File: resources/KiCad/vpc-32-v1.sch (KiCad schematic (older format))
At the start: 46 parts, among them J1 video out, J2 SD_SOCKET, J3 PS/2, J4 audio out, K1 jumper, P1 CONN_2, P2 ICSP, P3 XBUS, Q1 2N3906, Q2 2N3094, SW1 reset, U1 PIC32MX150F128B, U2 LM3940-3.3, X1 10Mhz

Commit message: ajout licence Creative Commons au projet KiCad
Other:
- note added: "Copyright 2013, Jacques Deschênes\nlicence Creative Commons: CC BY-SA"
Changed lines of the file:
@@
-EESchema Schematic File Version 2  date 2013-08-25 22:04:50
+EESchema Schematic File Version 2  date 2013-08-27 09:48:55
 LIBS:power
 LIBS:device
@@
 Sheet 1 1
 Title ""
-Date "26 aug 2013"
+Date "27 aug 2013"
 Rev ""
 Comp ""
@@
 Wire Wire Line
 	8550 1950 8550 2600
+Text Notes 7050 7050 0    59   ~ 0
+Copyright 2013, Jacques Deschênes\nlicence Creative Commons: CC BY-SA
 $EndSCHEMATC

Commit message: réglé bug avec interrupton TIMER 2
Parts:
- added D?: Power, symbol LED
- added D?: Status LED, symbol LED
- added R?: 150R, symbol R
- added R?: 220R, symbol R
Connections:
- net labels added: RB1, STATUS
- net labels removed: RB3, ~U2RTS
- wire segments 123 -> 128
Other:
- note added: "2"
- note removed: "1"
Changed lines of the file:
@@
-EESchema Schematic File Version 2  date 2013-08-27 09:48:55
+EESchema Schematic File Version 2  date 2013-08-28 16:27:26
 LIBS:power
 LIBS:device
@@
 Sheet 1 1
 Title ""
-Date "27 aug 2013"
+Date "28 aug 2013"
 Rev ""
 Comp ""
@@
 Connection ~ 4400 6150
 Wire Wire Line
-	2850 6150 4400 6150
+	2850 6150 4550 6150
 Wire Wire Line
 	8500 4700 8500 4900
@@
 RB0
 Text GLabel 6250 5800 0    39   Input ~ 0
-RB3
+RB1
 Text GLabel 6250 5900 0    39   Input ~ 0
 RB8
@@
 VPC-32
 Text Notes 10700 7650 0    59   ~ 0
-1
+2
 $Comp
 L R R8
@@
 Wire Wire Line
 	7850 1600 8050 1600
-Text GLabel 4950 3650 0    39   Input ~ 0
-~U2RTS
-Wire Wire Line
-	4950 3650 5100 3650
 $Comp
 L RJ11 J?
@@
 Text Notes 7050 7050 0    59   ~ 0
 Copyright 2013, Jacques Deschênes\nlicence Creative Commons: CC BY-SA
+$Comp
+L LED D?
+U 1 1 521E10B9
+P 5150 6350
+F 0 "D?" H 5150 6450 50  0000 C CNN
+F 1 "Power" H 5150 6250 50  0000 C CNN
+F 2 "" H 5150 6350 60  0000 C CNN
+F 3 "" H 5150 6350 60  0000 C CNN
+	1    5150 6350
+	0    1    1    0
+$EndComp
+$Comp
+L R R?
+U 1 1 521E10C8
+P 4800 6150
+F 0 "R?" V 4880 6150 50  0000 C CNN
+F 1 "150R" V 4800 6150 50  0000 C CNN
+F 2 "" H 4800 6150 60  0000 C CNN
+F 3 "" H 4800 6150 60  0000 C CNN
+	1    4800 6150
+	0    -1   -1   0
+$EndComp
+$Comp
+L GND #PWR?
+U 1 1 521E10D5
+P 5150 6650
+F 0 "#PWR?" H 5150 6650 30  0001 C CNN
+F 1 "GND" H 5150 6580 30  0001 C CNN
+F 2 "" H 5150 6650 60  0000 C CNN
+F 3 "" H 5150 6650 60  0000 C CNN
+	1    5150 6650
+	1    0    0    -1
+$EndComp
+Wire Wire Line
+	5050 6150 5150 6150
+Wire Wire Line
+	5150 6550 5150 6650
+$Comp
+L LED D?
+U 1 1 521E127D
+P 4200 5350
+F 0 "D?" H 4200 5450 50  0000 C CNN
+F 1 "Status LED" H 4200 5250 50  0000 C CNN
+F 2 "" H 4200 5350 60  0000 C CNN
+F 3 "" H 4200 5350 60  0000 C CNN
+	1    4200 5350
+	0    1    1    0
+$EndComp
+$Comp
+L R R?
+U 1 1 521E128C
+P 3950 5000
+F 0 "R?" V 4030 5000 50  0000 C CNN
+F 1 "220R" V 3950 5000 50  0000 C CNN
+F 2 "" H 3950 5000 60  0000 C CNN
+F 3 "" H 3950 5000 60  0000 C CNN
+	1    3950 5000
+	0    -1   -1   0
+$EndComp
+$Comp
+L GND #PWR?
+U 1 1 521E12A3
+P 4200 5650
+F 0 "#PWR?" H 4200 5650 30  0001 C CNN
+F 1 "GND" H 4200 5580 30  0001 C CNN
+F 2 "" H 4200 5650 60  0000 C CNN
+F 3 "" H 4200 5650 60  0000 C CNN
+	1    4200 5650
+	1    0    0    -1
+$EndComp
+Text GLabel 5050 3650 0    39   Input ~ 0
+STATUS
+Wire Wire Line
+	5100 3650 5050 3650
+Text GLabel 3600 5000 0    39   Input ~ 0
+STATUS
+Wire Wire Line
+	4200 5550 4200 5650
+Wire Wire Line
+	4200 5000 4200 5150
+Wire Wire Line
+	3700 5000 3600 5000
 $EndSCHEMATC

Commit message: modification au schéma électronique
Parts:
- removed R7: 10k, symbol R
- gave numbers to parts that had none: 5
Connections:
- net labels removed: V+
- wire segments 128 -> 129
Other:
- moved on the sheet: J5
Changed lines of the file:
@@
-EESchema Schematic File Version 2  date 2013-08-28 16:27:26
+EESchema Schematic File Version 2  date 2013-09-01 22:06:51
 LIBS:power
 LIBS:device
@@
 Sheet 1 1
 Title ""
-Date "28 aug 2013"
+Date "2 sep 2013"
 Rev ""
 Comp ""
@@
 $EndComp
 $Comp
-L GND #PWR6
+L GND #PWR01
 U 1 1 52181107
 P 3550 4650
-F 0 "#PWR6" H 3550 4650 30  0001 C CNN
+F 0 "#PWR01" H 3550 4650 30  0001 C CNN
 F 1 "GND" H 3550 4580 30  0001 C CNN
 F 2 "" H 3550 4650 60  0000 C CNN
@@
 $EndComp
 $Comp
-L GND #PWR9
+L GND #PWR02
 U 1 1 52181114
 P 4150 4650
-F 0 "#PWR9" H 4150 4650 30  0001 C CNN
+F 0 "#PWR02" H 4150 4650 30  0001 C CNN
 F 1 "GND" H 4150 4580 30  0001 C CNN
 F 2 "" H 4150 4650 60  0000 C CNN
@@
 $EndComp
 $Comp
-L GND #PWR17
+L GND #PWR03
 U 1 1 52181145
 P 8500 4900
-F 0 "#PWR17" H 8500 4900 30  0001 C CNN
+F 0 "#PWR03" H 8500 4900 30  0001 C CNN
 F 1 "GND" H 8500 4830 30  0001 C CNN
 F 2 "" H 8500 4900 60  0000 C CNN
@@
 +3,3V
 $Comp
-L GND #PWR14
+L GND #PWR04
 U 1 1 521812CB
 P 7000 4000
-F 0 "#PWR14" H 7000 4000 30  0001 C CNN
+F 0 "#PWR04" H 7000 4000 30  0001 C CNN
 F 1 "GND" H 7000 3930 30  0001 C CNN
 F 2 "" H 7000 4000 60  0000 C CNN
@@
 $EndComp
 $Comp
-L GND #PWR12
+L GND #PWR05
 U 1 1 521812EF
 P 4850 3750
-F 0 "#PWR12" H 4850 3750 30  0001 C CNN
+F 0 "#PWR05" H 4850 3750 30  0001 C CNN
 F 1 "GND" H 4850 3680 30  0001 C CNN
 F 2 "" H 4850 3750 60  0000 C CNN
@@
 $EndComp
 $Comp
-L GND #PWR8
+L GND #PWR06
 U 1 1 52181391
 P 3950 6650
-F 0 "#PWR8" H 3950 6650 30  0001 C CNN
+F 0 "#PWR06" H 3950 6650 30  0001 C CNN
 F 1 "GND" H 3950 6580 30  0001 C CNN
 F 2 "" H 3950 6650 60  0000 C CNN
@@
 $EndComp
 $Comp
-L GND #PWR10
+L GND #PWR07
 U 1 1 52181397
 P 4400 6650
-F 0 "#PWR10" H 4400 6650 30  0001 C CNN
+F 0 "#PWR07" H 4400 6650 30  0001 C CNN
 F 1 "GND" H 4400 6580 30  0001 C CNN
 F 2 "" H 4400 6650 60  0000 C CNN
@@
 $EndComp
 $Comp
-L GND #PWR5
+L GND #PWR08
 U 1 1 5218D55D
 P 3300 2800
-F 0 "#PWR5" H 3300 2800 30  0001 C CNN
+F 0 "#PWR08" H 3300 2800 30  0001 C CNN
 F 1 "GND" H 3300 2730 30  0001 C CNN
 F 2 "" H 3300 2800 60  0000 C CNN
@@
 $EndComp
 $Comp
-L GND #PWR15
+L GND #PWR09
 U 1 1 521A0F8C
 P 7400 4000
-F 0 "#PWR15" H 7400 4000 30  0001 C CNN
+F 0 "#PWR09" H 7400 4000 30  0001 C CNN
 F 1 "GND" H 7400 3930 30  0001 C CNN
 F 2 "" H 7400 4000 60  0000 C CNN
@@
 $EndComp
 $Comp
-L GND #PWR7
+L GND #PWR010
 U 1 1 521A102C
 P 3750 1800
-F 0 "#PWR7" H 3750 1800 30  0001 C CNN
+F 0 "#PWR010" H 3750 1800 30  0001 C CNN
 F 1 "GND" H 3750 1730 30  0001 C CNN
 F 2 "" H 3750 1800 60  0000 C CNN
@@
 $EndComp
 $Comp
-L GND #PWR11
+L GND #PWR011
 U 1 1 521A10AE
 P 4600 2450
-F 0 "#PWR11" H 4600 2450 30  0001 C CNN
+F 0 "#PWR011" H 4600 2450 30  0001 C CNN
 F 1 "GND" H 4600 2380 30  0001 C CNN
 F 2 "" H 4600 2450 60  0000 C CNN
@@
 $EndComp
 $Comp
-L GND #PWR4
+L GND #PWR012
 U 1 1 521A15C0
 P 3100 4800
-F 0 "#PWR4" H 3100 4800 30  0001 C CNN
+F 0 "#PWR012" H 3100 4800 30  0001 C CNN
 F 1 "GND" H 3100 4730 30  0001 C CNN
 F 2 "" H 3100 4800 60  0000 C CNN
@@
 	1    0    0    -1
 $EndComp
-Text GLabel 3250 4200 1    60   Input ~ 0
-V+
+Text GLabel 3250 4200 1    39   Input ~ 0
++3,3V
 Text GLabel 2750 4550 2    39   Input ~ 0
 SPI2/SDI
@@
 F 3 "" H 1750 3550 60  0000 C CNN
 	1    1750 3550
-	1    0    0    -1
-$EndComp
-$Comp
-L R R7
-U 1 1 521A1B35
-P 2150 3550
-F 0 "R7" V 2230 3550 50  0000 C CNN
-F 1 "10k" V 2150 3550 50  0000 C CNN
-F 2 "" H 2150 3550 60  0000 C CNN
-F 3 "" H 2150 3550 60  0000 C CNN
-	1    2150 3550
 	1    0    0    -1
 $EndComp
@@
 +3,3V
 $Comp
-L GND #PWR13
+L GND #PWR013
 U 1 1 521A28F4
 P 6000 1650
-F 0 "#PWR13" H 6000 1650 30  0001 C CNN
+F 0 "#PWR013" H 6000 1650 30  0001 C CNN
 F 1 "GND" H 6000 1580 30  0001 C CNN
 F 2 "" H 6000 1650 60  0000 C CNN
@@
 PGEC1
 $Comp
-L GND #PWR22
+L GND #PWR014
 U 1 1 521A78A1
 P 9750 2600
-F 0 "#PWR22" H 9750 2600 30  0001 C CNN
+F 0 "#PWR014" H 9750 2600 30  0001 C CNN
 F 1 "GND" H 9750 2530 30  0001 C CNN
 F 2 "" H 9750 2600 60  0000 C CNN
@@
 Wire Wire Line
 	1750 3300 1750 3200
-Wire Wire Line
-	1750 3300 2150 3300
 Wire Wire Line
 	1750 4750 2150 4750
@@
 $EndComp
 Wire Wire Line
-	9750 2300 9050 2300
-Wire Wire Line
 	8850 2800 9050 2800
 $Comp
@@
 $EndComp
 $Comp
-L GND #PWR19
+L GND #PWR015
 U 1 1 521A7A94
 P 8550 3100
-F 0 "#PWR19" H 8550 3100 30  0001 C CNN
+F 0 "#PWR015" H 8550 3100 30  0001 C CNN
 F 1 "GND" H 8550 3030 30  0001 C CNN
 F 2 "" H 8550 3100 60  0000 C CNN
@@
 $EndComp
 $Comp
-L GND #PWR23
+L GND #PWR016
 U 1 1 521A7A9A
 P 9550 2950
-F 0 "#PWR23" H 9550 2950 30  0001 C CNN
+F 0 "#PWR016" H 9550 2950 30  0001 C CNN
 F 1 "GND" H 9550 2880 30  0001 C CNN
 F 2 "" H 9550 2950 60  0000 C CNN
@@
 	7850 2300 8650 2300
 $Comp
-L GND #PWR18
+L GND #PWR017
 U 1 1 521A7BF6
 P 8150 2850
-F 0 "#PWR18" H 8150 2850 30  0001 C CNN
+F 0 "#PWR017" H 8150 2850 30  0001 C CNN
 F 1 "GND" H 8150 2780 30  0001 C CNN
 F 2 "" H 8150 2850 60  0000 C CNN
@@
 TX
 Connection ~ 7850 1600
-Text GLabel 9600 2150 0    39   Input ~ 0
+Text GLabel 9550 2000 0    39   Input ~ 0
 TX
 Text GLabel 6700 3750 2    39   Input ~ 0
@@
 $EndComp
 $Comp
-L GND #PWR24
+L GND #PWR018
 U 1 1 521A9812
 P 10500 6350
-F 0 "#PWR24" H 10500 6350 30  0001 C CNN
+F 0 "#PWR018" H 10500 6350 30  0001 C CNN
 F 1 "GND" H 10500 6280 30  0001 C CNN
 F 2 "" H 10500 6350 60  0000 C CNN
@@
 	10500 6200 10500 6350
 $Comp
-L GND #PWR21
+L GND #PWR019
 U 1 1 521A9A38
 P 9750 6450
-F 0 "#PWR21" H 9750 6450 30  0001 C CNN
+F 0 "#PWR019" H 9750 6450 30  0001 C CNN
 F 1 "GND" H 9750 6380 30  0001 C CNN
 F 2 "" H 9750 6450 60  0000 C CNN
@@
 $EndComp
 $Comp
-L GND #PWR20
+L GND #PWR020
 U 1 1 521A9A3E
 P 9250 6450
-F 0 "#PWR20" H 9250 6450 30  0001 C CNN
+F 0 "#PWR020" H 9250 6450 30  0001 C CNN
 F 1 "GND" H 9250 6380 30  0001 C CNN
 F 2 "" H 9250 6450 60  0000 C CNN
@@
 $EndComp
 $Comp
-L GND #PWR16
+L GND #PWR021
 U 1 1 521A9A4E
 P 8450 6450
-F 0 "#PWR16" H 8450 6450 30  0001 C CNN
+F 0 "#PWR021" H 8450 6450 30  0001 C CNN
 F 1 "GND" H 8450 6380 30  0001 C CNN
 F 2 "" H 8450 6450 60  0000 C CNN
@@
 $EndComp
 $Comp
-L GND #PWR3
+L GND #PWR022
 U 1 1 521A9D5C
 P 2700 6400
-F 0 "#PWR3" H 2700 6400 30  0001 C CNN
+F 0 "#PWR022" H 2700 6400 30  0001 C CNN
 F 1 "GND" H 2700 6330 30  0001 C CNN
 F 2 "" H 2700 6400 60  0000 C CNN
@@
 $EndComp
 $Comp
-L GND #PWR1
+L GND #PWR023
 U 1 1 521A9ED6
 P 1650 6500
-F 0 "#PWR1" H 1650 6500 30  0001 C CNN
+F 0 "#PWR023" H 1650 6500 30  0001 C CNN
 F 1 "GND" H 1650 6430 30  0001 C CNN
 F 2 "" H 1650 6500 60  0000 C CNN
@@
 $EndComp
 $Comp
-L GND #PWR2
+L GND #PWR024
 U 1 1 521AA1E5
 P 1900 6650
-F 0 "#PWR2" H 1900 6650 30  0001 C CNN
+F 0 "#PWR024" H 1900 6650 30  0001 C CNN
 F 1 "GND" H 1900 6580 30  0001 C CNN
 F 2 "" H 1900 6650 60  0000 C CNN
@@
 	7850 1600 8050 1600
 $Comp
-L RJ11 J?
+L RJ11 J5
 U 1 1 521AB1B3
-P 10350 2200
-F 0 "J?" H 10350 1850 60  0000 C CNN
-F 1 "RJ11" H 10300 2550 60  0000 C CNN
-F 2 "" H 10350 2200 60  0000 C CNN
-F 3 "" H 10350 2200 60  0000 C CNN
-	1    10350 2200
-	-1   0    0    1
+P 10350 2250
+F 0 "J5" H 10350 1900 60  0000 C CNN
+F 1 "RJ11" H 10300 2600 60  0000 C CNN
+F 2 "" H 10350 2250 60  0000 C CNN
+F 3 "" H 10350 2250 60  0000 C CNN
+	1    10350 2250
+	-1   0    0    -1
 $EndComp
 Wire Wire Line
 	9750 2600 9750 2450
 Wire Wire Line
-	9750 2150 9600 2150
+	9050 2150 9750 2150
 Wire Wire Line
 	8550 1950 8550 2600
@@
 Copyright 2013, Jacques Deschênes\nlicence Creative Commons: CC BY-SA
 $Comp
-L LED D?
+L LED D5
 U 1 1 521E10B9
 P 5150 6350
-F 0 "D?" H 5150 6450 50  0000 C CNN
+F 0 "D5" H 5150 6450 50  0000 C CNN
 F 1 "Power" H 5150 6250 50  0000 C CNN
 F 2 "" H 5150 6350 60  0000 C CNN
@@
 $EndComp
 $Comp
-L R R?
+L R R19
 U 1 1 521E10C8
 P 4800 6150
-F 0 "R?" V 4880 6150 50  0000 C CNN
+F 0 "R19" V 4880 6150 50  0000 C CNN
 F 1 "150R" V 4800 6150 50  0000 C CNN
 F 2 "" H 4800 6150 60  0000 C CNN
@@
 $EndComp
 $Comp
-L GND #PWR?
+L GND #PWR025
 U 1 1 521E10D5
 P 5150 6650
-F 0 "#PWR?" H 5150 6650 30  0001 C CNN
+F 0 "#PWR025" H 5150 6650 30  0001 C CNN
 F 1 "GND" H 5150 6580 30  0001 C CNN
 F 2 "" H 5150 6650 60  0000 C CNN
@@
 	5150 6550 5150 6650
 $Comp
-L LED D?
+L LED D4
 U 1 1 521E127D
 P 4200 5350
-F 0 "D?" H 4200 5450 50  0000 C CNN
+F 0 "D4" H 4200 5450 50  0000 C CNN
 F 1 "Status LED" H 4200 5250 50  0000 C CNN
 F 2 "" H 4200 5350 60  0000 C CNN
@@
 $EndComp
 $Comp
-L R R?
+L R R18
 U 1 1 521E128C
 P 3950 5000
-F 0 "R?" V 4030 5000 50  0000 C CNN
+F 0 "R18" V 4030 5000 50  0000 C CNN
 F 1 "220R" V 3950 5000 50  0000 C CNN
 F 2 "" H 3950 5000 60  0000 C CNN
@@
 $EndComp
 $Comp
-L GND #PWR?
+L GND #PWR026
 U 1 1 521E12A3
 P 4200 5650
-F 0 "#PWR?" H 4200 5650 30  0001 C CNN
+F 0 "#PWR026" H 4200 5650 30  0001 C CNN
 F 1 "GND" H 4200 5580 30  0001 C CNN
 F 2 "" H 4200 5650 60  0000 C CNN
@@
 Wire Wire Line
 	3700 5000 3600 5000
+Wire Wire Line
+	2150 3800 1750 3800
+Wire Wire Line
+	9550 2000 9750 2000
+Wire Wire Line
+	9050 2300 9050 2150
 $EndSCHEMATC

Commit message: ajout photos prototype
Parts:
- removed P3: XBUS, symbol CONN_6
- added P3: XBUS, symbol CONN_5
- added R?: 22k, symbol R
- R6: value 10k -> 22k
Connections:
- net labels added: SDO2
- net labels removed: RB8
- wire segments 129 -> 131
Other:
- moved on the sheet: R6

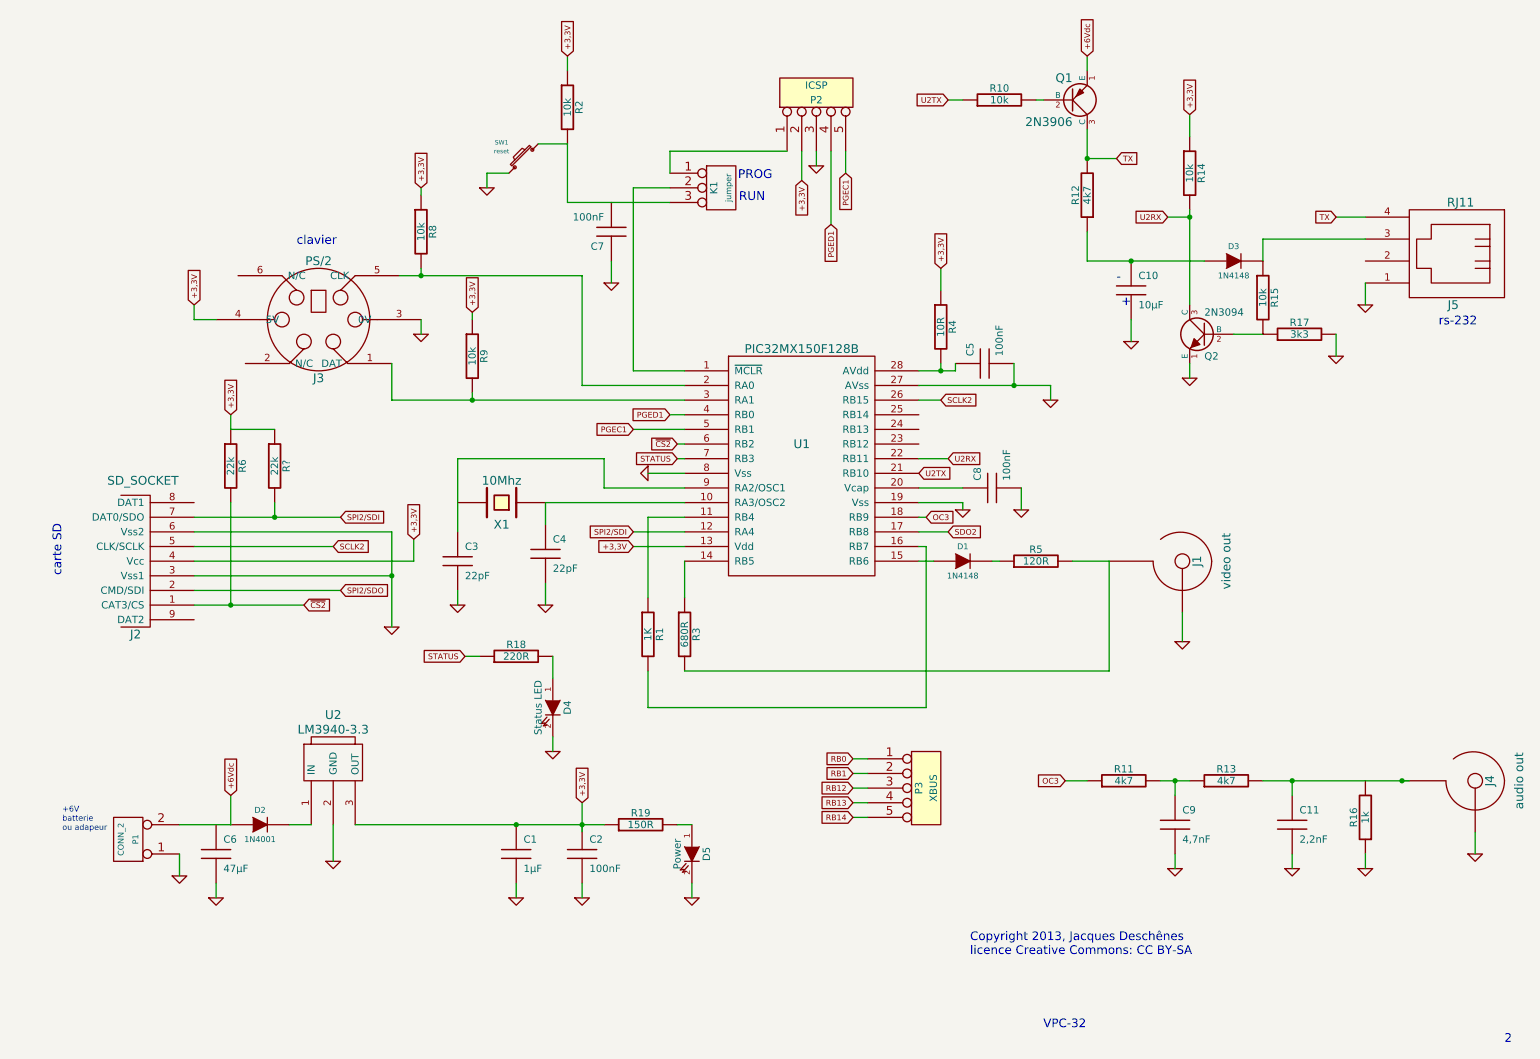
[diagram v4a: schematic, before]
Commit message: modification au schéma électronique, test interface RS-232
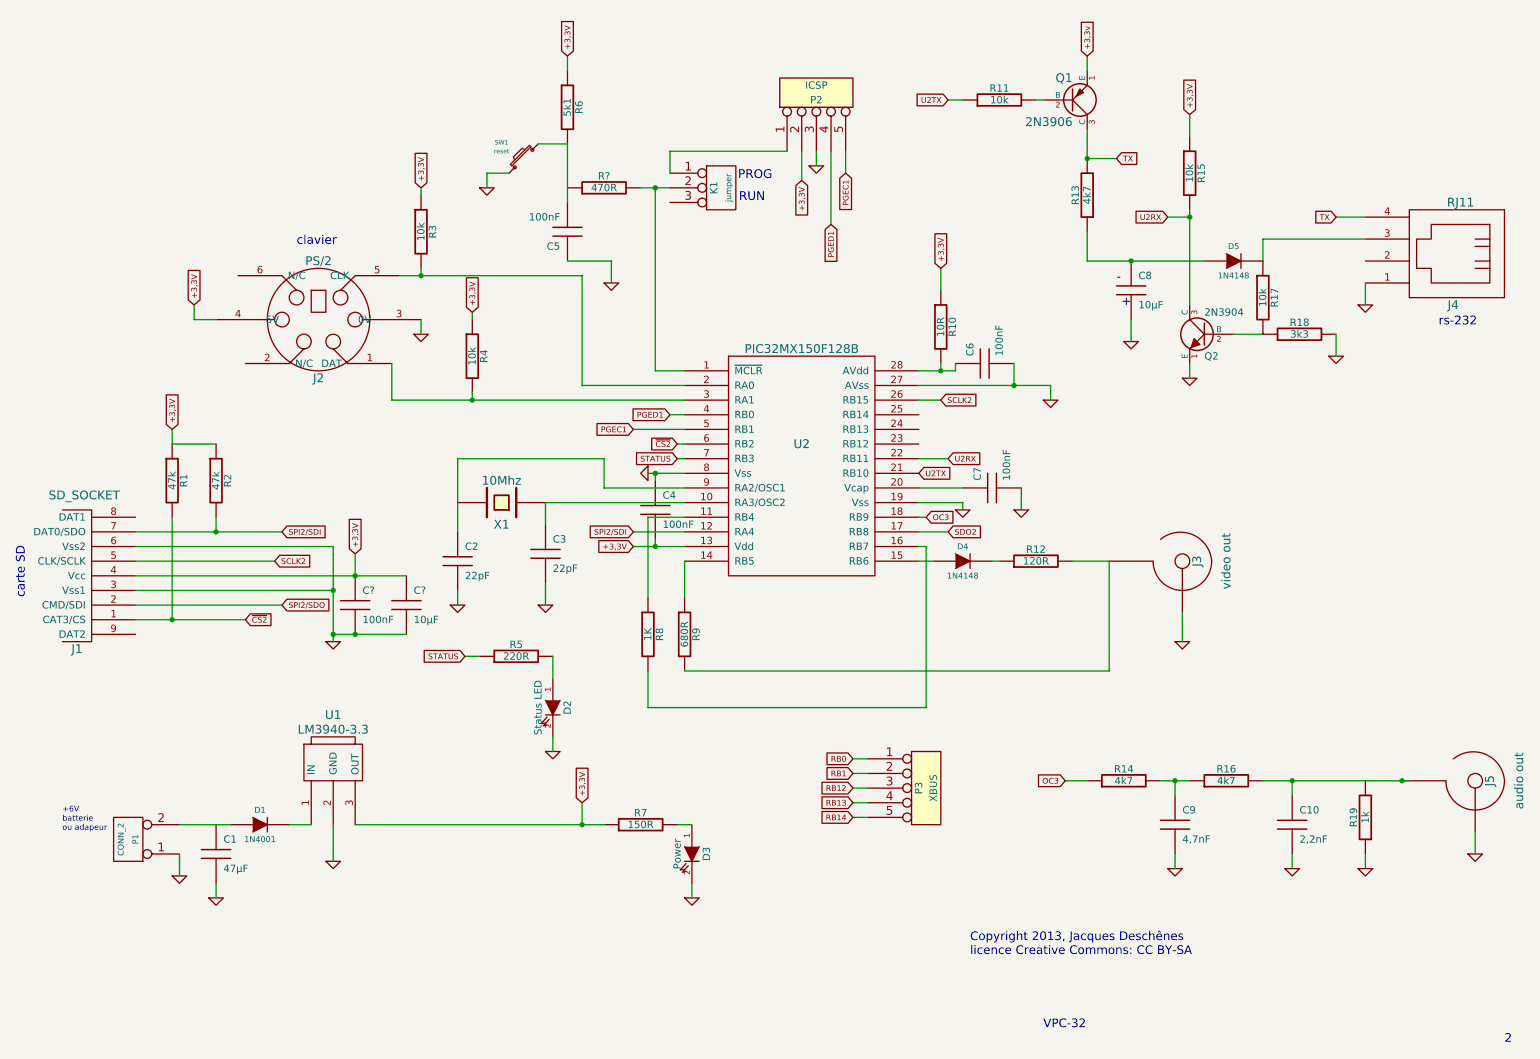
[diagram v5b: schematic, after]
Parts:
- removed C1: 1µF, symbol C
- added C?: 100nF, symbol C
- added C?: 10µF, symbol C
- added R?: 470R, symbol R
- Q2: value 2N3094 -> 2N3904
- R1: renamed from R6; value 22k -> 47k
- R2: renamed from R?; value 22k -> 47k
- R6: renamed from R2; value 10k -> 5k1
- renumbered C6 to C1, C11 to C10, C3 to C2, C4 to C3, C2 to C4, C7 to C5, C5 to C6, C8 to C7, C10 to C8, D2 to D1, D4 to D2, D5 to D3, D1 to D4, D3 to D5, J2 to J1, J3 to J2, J1 to J3, J5 to J4, J4 to J5, R4 to R10, R10 to R11, R5 to R12, R12 to R13, R11 to R14, R14 to R15, R13 to R16, R15 to R17, R17 to R18, R16 to R19, R8 to R3, R9 to R4, R18 to R5, R19 to R7, R1 to R8, R3 to R9, U2 to U1, U1 to U2
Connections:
- net +3,3V: now also C4.2, C?.1, C?.1; no longer C4.1
- net GND: now also C4.1, C?.2, C?.2; no longer C4.2
- net at K1.2 (PM), U2.1 (~MCLR): now also R?.2
- net at R6.2, SW1.1: now also C5.2; no longer K1.3 (P3)
- net +6Vdc: no longer names the net of D1.1 (A), P1.2 (PM)
- net +6Vdc: no longer Q1.1 (E)
- new net +3,3v: Q1.1 (E)
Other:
- moved on the sheet: C4, C5, J1, R1, R2

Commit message: travail sur graphics.c
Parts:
- R6: value 5k1 -> 22k
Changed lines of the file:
@@
-EESchema Schematic File Version 2  date 2013-09-05 09:54:04
+EESchema Schematic File Version 2  date 2013-10-02 07:50:32
 LIBS:power
 LIBS:device
@@
 Sheet 1 1
 Title ""
-Date "5 sep 2013"
+Date "2 oct 2013"
 Rev ""
 Comp ""
@@
 P 4300 1250
 F 0 "R6" V 4380 1250 50  0000 C CNN
-F 1 "5k1" V 4300 1250 50  0000 C CNN
+F 1 "22k" V 4300 1250 50  0000 C CNN
 F 2 "" H 4300 1250 60  0000 C CNN
 F 3 "" H 4300 1250 60  0000 C CNN

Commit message: work on shell
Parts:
- removed P1: CONN_2, symbol CONN_2
- added CON1: Power jack, symbol BARREL_JACK
- added F1: 500mA, symbol FUSE
- added SW2: Power, symbol SWITCH_INV
- gave numbers to parts that had none: 3
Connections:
- net GND: now also CON1.2
- net at D1.1 (A): now also F1.2
- new net: F1.1, SW2.3
- new net: CON1.1, SW2.2
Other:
- note added: "OFF"
- note added: "ON"
- note removed: "+6V\nbatterie\nou adapeur"
- moved on the sheet: C1, D1, D3, R7, U1
